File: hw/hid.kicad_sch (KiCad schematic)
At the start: 108 parts, among them M1 SK8701-01-004-MODULE, M2 SK8701-01-004-SENSOR, SW1 SW_Push, SW10 SW_Push, SW11 SW_Push, SW12 SW_Push, SW13 SW_Push, SW14 SW_Push, SW15 SW_Push, SW16 SW_Push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

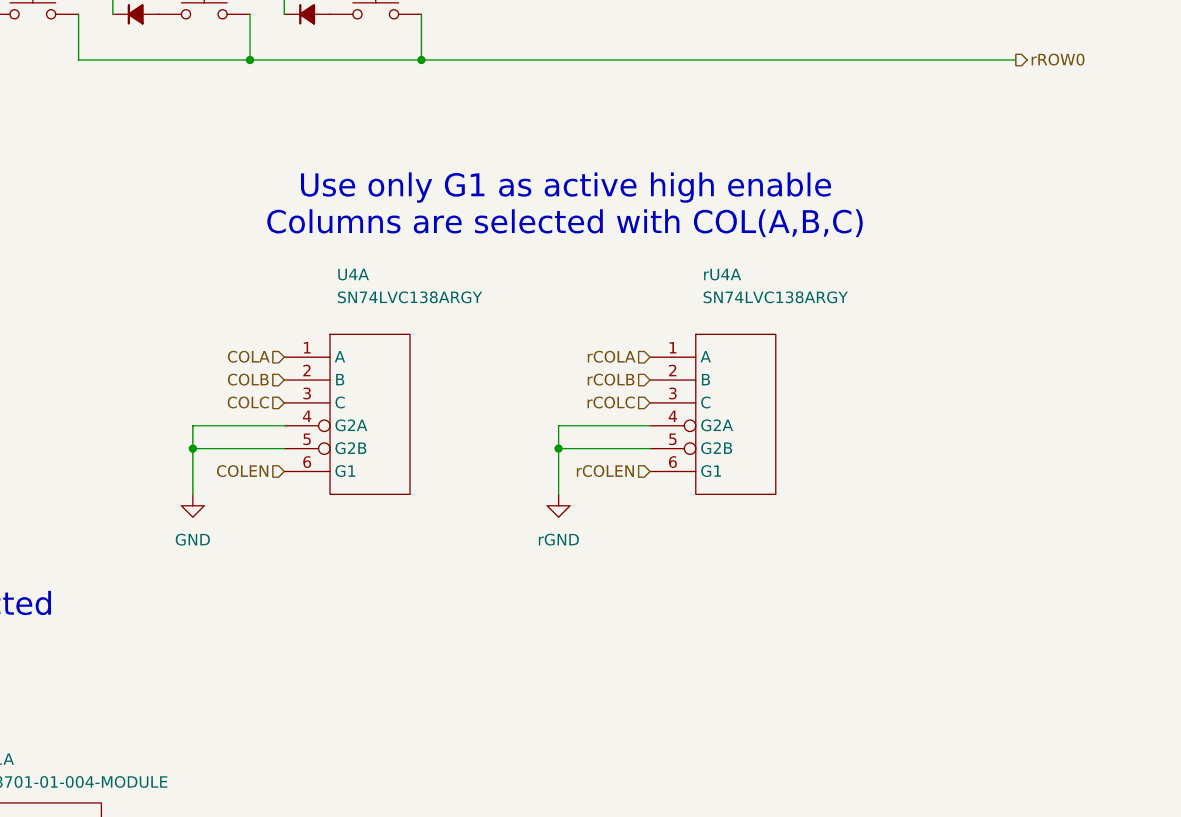
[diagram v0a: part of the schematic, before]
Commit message: Place and connect trackpoint module
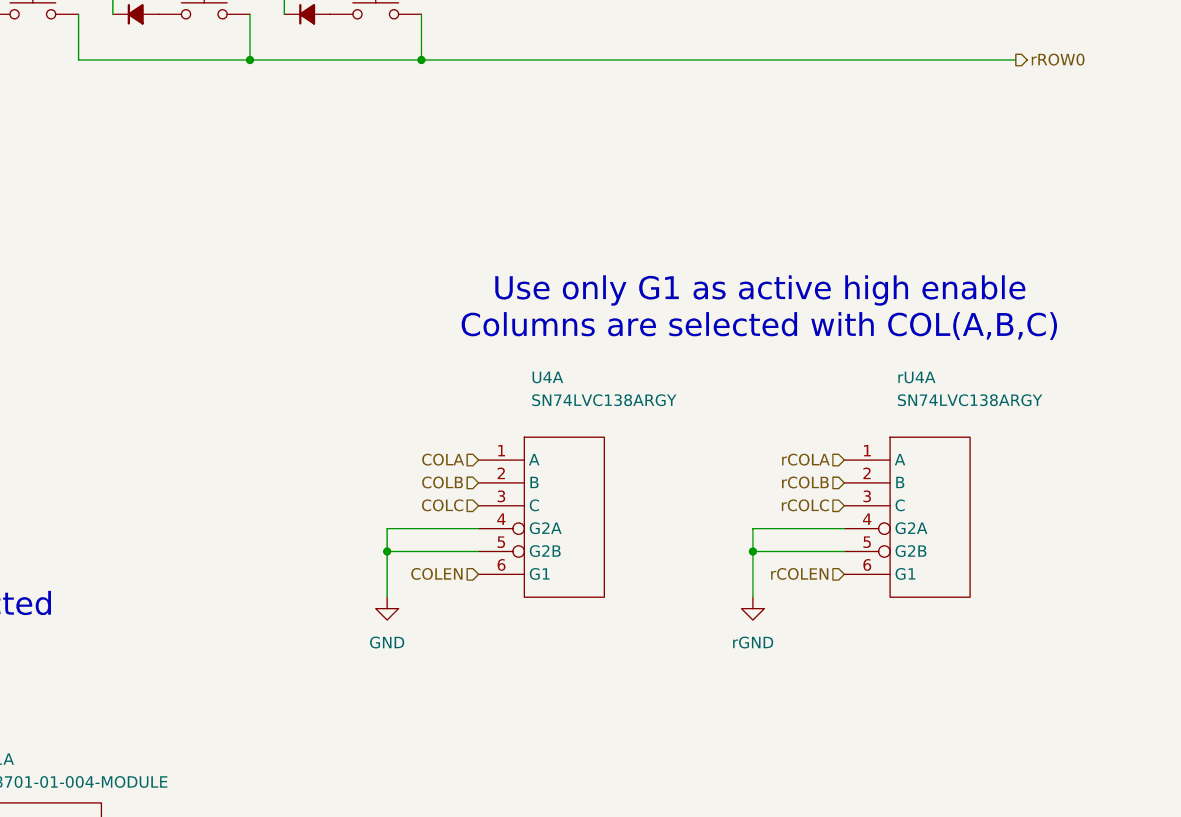
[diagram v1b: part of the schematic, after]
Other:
- moved on the sheet: U4A, rU4A
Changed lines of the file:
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@@
 	(text "Use only G1 as active high enable\nColumns are selected with COL(A,B,C)"
 		(exclude_from_sim no)
-		(at 327.152 138.176 0)
+		(at 348.742 149.606 0)
 		(effects
 			(font
@@
 	)
 	(junction
-		(at 285.75 165.1)
+		(at 307.34 176.53)
 		(diameter 0)
 		(color 0 0 0 0)
@@
 	)
 	(junction
-		(at 326.39 165.1)
+		(at 347.98 176.53)
 		(diameter 0)
 		(color 0 0 0 0)
@@
 	(wire
 		(pts
-			(xy 326.39 162.56) (xy 326.39 165.1)
+			(xy 347.98 173.99) (xy 347.98 176.53)
 		)
 		(stroke
@@
 	(wire
 		(pts
-			(xy 336.55 162.56) (xy 326.39 162.56)
+			(xy 358.14 173.99) (xy 347.98 173.99)
 		)
 		(stroke
@@
 	(wire
 		(pts
-			(xy 285.75 165.1) (xy 295.91 165.1)
+			(xy 307.34 176.53) (xy 317.5 176.53)
 		)
 		(stroke
@@
 	(wire
 		(pts
-			(xy 285.75 162.56) (xy 285.75 165.1)
+			(xy 307.34 173.99) (xy 307.34 176.53)
 		)
 		(stroke
@@
 	(wire
 		(pts
-			(xy 326.39 165.1) (xy 326.39 170.18)
+			(xy 347.98 176.53) (xy 347.98 181.61)
 		)
 		(stroke
@@
 	(wire
 		(pts
-			(xy 285.75 165.1) (xy 285.75 170.18)
+			(xy 307.34 176.53) (xy 307.34 181.61)
 		)
 		(stroke
@@
 	(wire
 		(pts
-			(xy 326.39 165.1) (xy 336.55 165.1)
+			(xy 347.98 176.53) (xy 358.14 176.53)
 		)
 		(stroke
@@
 	(wire
 		(pts
-			(xy 295.91 162.56) (xy 285.75 162.56)
+			(xy 317.5 173.99) (xy 307.34 173.99)
 		)
 		(stroke
@@
 	(hierarchical_label "rCOLEN"
 		(shape input)
-		(at 336.55 167.64 180)
+		(at 358.14 179.07 180)
 		(effects
 			(font
@@
 	(hierarchical_label "rCOLC"
 		(shape input)
-		(at 336.55 160.02 180)
+		(at 358.14 171.45 180)
 		(effects
 			(font
@@
 	(hierarchical_label "COLEN"
 		(shape input)
-		(at 295.91 167.64 180)
+		(at 317.5 179.07 180)
 		(effects
 			(font
@@
 	(hierarchical_label "rCOLB"
 		(shape input)
-		(at 336.55 157.48 180)
+		(at 358.14 168.91 180)
 		(effects
 			(font
@@
 	(hierarchical_label "rCOLA"
 		(shape input)
-		(at 336.55 154.94 180)
+		(at 358.14 166.37 180)
 		(effects
 			(font
@@
 	(hierarchical_label "COLA"
 		(shape input)
-		(at 295.91 154.94 180)
+		(at 317.5 166.37 180)
 		(effects
 			(font
@@
 	(hierarchical_label "COLB"
 		(shape input)
-		(at 295.91 157.48 180)
+		(at 317.5 168.91 180)
 		(effects
 			(font
@@
 	(hierarchical_label "COLC"
 		(shape input)
-		(at 295.91 160.02 180)
+		(at 317.5 171.45 180)
 		(effects
 			(font
@@
 		)
 		(instances
-			(project ""
+			(project "alidade"
 				(path "/4cc5d416-57f5-4147-8183-e03ae6b1198a/2e72dd0e-817e-4022-b409-1f79b0de6857"
 					(reference "U4")
@@
 		)
 		(instances
-			(project ""
+			(project "alidade"
 				(path "/4cc5d416-57f5-4147-8183-e03ae6b1198a/2e72dd0e-817e-4022-b409-1f79b0de6857"
 					(reference "#r3V3_03")
@@
 		)
 		(instances
-			(project ""
+			(project "alidade"
 				(path "/4cc5d416-57f5-4147-8183-e03ae6b1198a/2e72dd0e-817e-4022-b409-1f79b0de6857"
 					(reference "R8")
@@
 		)
 		(instances
-			(project ""
+			(project "alidade"
 				(path "/4cc5d416-57f5-4147-8183-e03ae6b1198a/2e72dd0e-817e-4022-b409-1f79b0de6857"
 					(reference "U4")
@@
 		)
 		(instances
-			(project ""
+			(project "alidade"
 				(path "/4cc5d416-57f5-4147-8183-e03ae6b1198a/2e72dd0e-817e-4022-b409-1f79b0de6857"
 					(reference "#GND07")
@@
 	(symbol
 		(lib_id "Alidade:SN74LVC138ARGY")
-		(at 295.91 152.4 0)
+		(at 317.5 163.83 0)
 		(unit 1)
 		(exclude_from_sim no)
@@
 		(dnp no)
 		(property "Reference" "U4"
-			(at 301.752 145.796 0)
+			(at 323.342 157.226 0)
 			(effects
 				(font
@@
 		)
 		(property "Value" "SN74LVC138ARGY"
-			(at 301.752 148.336 0)
+			(at 323.342 159.766 0)
 			(effects
 				(font
@@
 		)
 		(property "Footprint" ""
-			(at 295.91 152.4 0)
+			(at 317.5 163.83 0)
 			(effects
 				(font
@@
 		)
 		(property "Datasheet" ""
-			(at 295.91 152.4 0)
+			(at 317.5 163.83 0)
 			(effects
 				(font
@@
 		)
 		(property "Description" ""
-			(at 295.91 152.4 0)
+			(at 317.5 163.83 0)
 			(effects
 				(font
@@
 		)
 		(instances
-			(project ""
+			(project "alidade"
 				(path "/4cc5d416-57f5-4147-8183-e03ae6b1198a/2e72dd0e-817e-4022-b409-1f79b0de6857"
 					(reference "U4")
@@
 		)
 		(instances
-			(project ""
+			(project "alidade"
 				(path "/4cc5d416-57f5-4147-8183-e03ae6b1198a/2e72dd0e-817e-4022-b409-1f79b0de6857"
 					(reference "#rGND08")
@@
 	(symbol
 		(lib_id "Alidade:SN74LVC138ARGY")
-		(at 336.55 152.4 0)
+		(at 358.14 163.83 0)
 		(unit 1)
 		(exclude_from_sim no)
@@
 		(dnp no)
 		(property "Reference" "rU4"
-			(at 342.392 145.796 0)
+			(at 363.982 157.226 0)
 			(effects
 				(font
@@
 		)
 		(property "Value" "SN74LVC138ARGY"
-			(at 342.392 148.336 0)
+			(at 363.982 159.766 0)
 			(effects
 				(font
@@
 		)
 		(property "Footprint" ""
-			(at 336.55 152.4 0)
+			(at 358.14 163.83 0)
 			(effects
 				(font
@@
 		)
 		(property "Datasheet" ""
-			(at 336.55 152.4 0)
+			(at 358.14 163.83 0)
 			(effects
 				(font
@@
 		)
 		(property "Description" ""
-			(at 336.55 152.4 0)
+			(at 358.14 163.83 0)
 			(effects
 				(font
@@
 		)
 		(instances
-			(project ""
+			(project "alidade"
 				(path "/4cc5d416-57f5-4147-8183-e03ae6b1198a/2e72dd0e-817e-4022-b409-1f79b0de6857"
 					(reference "#1V8_04")
@@
 		)
 		(instances
-			(project ""
+			(project "alidade"
 				(path "/4cc5d416-57f5-4147-8183-e03ae6b1198a/2e72dd0e-817e-4022-b409-1f79b0de6857"
 					(reference "#r1V8_05")
@@
 		)
 		(instances
-			(project ""
+			(project "alidade"
 				(path "/4cc5d416-57f5-4147-8183-e03ae6b1198a/2e72dd0e-817e-4022-b409-1f79b0de6857"
 					(reference "M1")
@@
 		)
 		(instances
-			(project ""
+			(project "alidade"
 				(path "/4cc5d416-57f5-4147-8183-e03ae6b1198a/2e72dd0e-817e-4022-b409-1f79b0de6857"
 					(reference "#GND010")
@@
 	(symbol
 		(lib_id "Alidade:rGND")
-		(at 326.39 170.18 0)
+		(at 347.98 181.61 0)
 		(unit 1)
 		(exclude_from_sim no)
@@
 		(fields_autoplaced yes)
 		(property "Reference" "#rGND07"
-			(at 326.39 176.53 0)
+			(at 347.98 187.96 0)
 			(effects
 				(font
@@
 		)
 		(property "Value" "rGND"
-			(at 326.39 175.26 0)
+			(at 347.98 186.69 0)
 			(effects
 				(font
@@
 		)
 		(property "Footprint" ""
-			(at 326.39 170.18 0)
+			(at 347.98 181.61 0)
 			(effects
 				(font
@@
 		)
 		(property "Datasheet" ""
-			(at 326.39 170.18 0)
+			(at 347.98 181.61 0)
 			(effects
 				(font
@@
 		)
 		(property "Description" ""
-			(at 326.39 170.18 0)
+			(at 347.98 181.61 0)
 			(effects
 				(font
@@
 		)
 		(instances
-			(project ""
+			(project "alidade"
 				(path "/4cc5d416-57f5-4147-8183-e03ae6b1198a/2e72dd0e-817e-4022-b409-1f79b0de6857"
 					(reference "#rGND07")
@@
 		)
 		(instances
-			(project ""
+			(project "alidade"
 				(path "/4cc5d416-57f5-4147-8183-e03ae6b1198a/2e72dd0e-817e-4022-b409-1f79b0de6857"
 					(reference "#rGND011")
@@
 	(symbol
 		(lib_id "Alidade:GND")
-		(at 285.75 170.18 0)
+		(at 307.34 181.61 0)
 		(unit 1)
 		(exclude_from_sim no)
@@
 		(fields_autoplaced yes)
 		(property "Reference" "#GND05"
-			(at 285.75 176.53 0)
+			(at 307.34 187.96 0)
 			(effects
 				(font
@@
 		)
 		(property "Value" "GND"
-			(at 285.75 175.26 0)
+			(at 307.34 186.69 0)
 			(effects
 				(font
@@
 		)
 		(property "Footprint" ""
-			(at 285.75 170.18 0)
+			(at 307.34 181.61 0)
 			(effects
 				(font
@@
 		)
 		(property "Datasheet" ""
-			(at 285.75 170.18 0)
+			(at 307.34 181.61 0)
 			(effects
 				(font
@@
 		)
 		(property "Description" ""
-			(at 285.75 170.18 0)
+			(at 307.34 181.61 0)
 			(effects
 				(font
@@
 		)
 		(instances
-			(project ""
+			(project "alidade"
 				(path "/4cc5d416-57f5-4147-8183-e03ae6b1198a/2e72dd0e-817e-4022-b409-1f79b0de6857"
 					(reference "#GND05")
@@
 		)
 		(instances
-			(project ""
+			(project "alidade"
 				(path "/4cc5d416-57f5-4147-8183-e03ae6b1198a/2e72dd0e-817e-4022-b409-1f79b0de6857"
 					(reference "#3V3_03")
@@
 		)
 		(instances
-			(project ""
+			(project "alidade"
 				(path "/4cc5d416-57f5-4147-8183-e03ae6b1198a/2e72dd0e-817e-4022-b409-1f79b0de6857"
 					(reference "M1")
@@
 		)
 		(instances
-			(project ""
+			(project "alidade"
 				(path "/4cc5d416-57f5-4147-8183-e03ae6b1198a/2e72dd0e-817e-4022-b409-1f79b0de6857"
 					(reference "M2")

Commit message: Debug header
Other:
- title: (none) -> Alidade
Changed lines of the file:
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@@
 	(generator_version "9.0")
 	(paper "A3")
+	(title_block
+		(title "Alidade")
+		(date "2026-03-29")
+		(rev "1.0.0rc1")
+	)
 	(text "Need pull ups on rows?"
 		(exclude_from_sim no)
